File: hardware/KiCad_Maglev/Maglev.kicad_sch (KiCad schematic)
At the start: 32 parts, among them J1 USB_C_Receptacle, J2 691103110002, J3 61300621121, J4 61300821121, U1 WE-TVS-82400102, U2 ESP32-C3

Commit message: Update Rooting ESP32
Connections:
- net +USB_D: no longer U1.3, U2.25 (GPIO18/USB_D-)
- net -USB_D: no longer U1.4, U2.26 (GPIO19/USB_D+)
- new net USB_D+: U1.3, U2.25 (GPIO18/USB_D-)
- new net USB_D-: U1.4, U2.26 (GPIO19/USB_D+)
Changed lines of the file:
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@@
 	)
 	(label "I2C_INT"
-		(at 152.4 114.3 180)
+		(at 156.21 120.65 180)
 		(effects
 			(font
@@
 		)
 	)
-	(label "-USB_D"
+	(label "USB_D-"
 		(at 80.01 161.29 0)
 		(effects
@@
 	)
 	(label "EM_B_P"
-		(at 152.4 86.36 180)
+		(at 156.21 92.71 180)
 		(effects
 			(font
@@
 	)
 	(label "EM_A_N"
-		(at 152.4 81.28 180)
+		(at 156.21 87.63 180)
 		(effects
 			(font
@@
 	)
 	(label "EM_B_N"
-		(at 152.4 88.9 180)
+		(at 156.21 95.25 180)
 		(effects
 			(font
@@
 	)
 	(label "I2C_SDA"
-		(at 152.4 119.38 180)
+		(at 156.21 125.73 180)
 		(effects
 			(font
@@
 	)
 	(label "EM_C_N"
-		(at 152.4 96.52 180)
+		(at 156.21 102.87 180)
 		(effects
 			(font
@@
 		)
 	)
-	(label "+USB_D"
+	(label "USB_D+"
 		(at 81.28 179.07 0)
 		(effects
@@
 	)
 	(label "I2C_SCL"
-		(at 152.4 116.84 180)
+		(at 156.21 123.19 180)
 		(effects
 			(font
@@
 		)
 	)
-	(label "+USB_D"
+	(label "USB_D+"
 		(at 120.65 34.29 0)
 		(effects
@@
 	)
 	(label "EM_D_P"
-		(at 152.4 101.6 180)
+		(at 156.21 107.95 180)
 		(effects
 			(font
@@
 		)
 	)
-	(label "-USB_D"
+	(label "USB_D-"
 		(at 120.65 31.75 0)
 		(effects
@@
 	)
 	(label "EM_A_P"
-		(at 152.4 78.74 180)
+		(at 156.21 85.09 180)
 		(effects
 			(font
@@
 	)
 	(label "EM_C_P"
-		(at 152.4 93.98 180)
+		(at 156.21 100.33 180)
 		(effects
 			(font
@@
 	)
 	(label "EM_D_N"
-		(at 152.4 104.14 180)
+		(at 156.21 110.49 180)
 		(effects
 			(font
@@
 	(symbol
 		(lib_id "power:+3.3V")
-		(at 152.4 109.22 90)
+		(at 156.21 115.57 90)
 		(unit 1)
 		(body_style 1)
@@
 		(fields_autoplaced yes)
 		(property "Reference" "#PWR058"
-			(at 156.21 109.22 0)
+			(at 160.02 115.57 0)
 			(hide yes)
 			(show_name no)
@@
 		)
 		(property "Value" "+3.3V"
-			(at 148.59 109.22 90)
+			(at 152.4 115.57 90)
 			(show_name no)
 			(do_not_autoplace no)
@@
 		)
 		(property "Footprint" ""
-			(at 152.4 109.22 0)
+			(at 156.21 115.57 0)
 			(hide yes)
 			(show_name no)
@@
 		)
 		(property "Datasheet" ""
-			(at 152.4 109.22 0)
+			(at 156.21 115.57 0)
 			(hide yes)
 			(show_name no)
@@
 		)
 		(property "Description" "Power symbol creates a global label with name \"+3.3V\""
-			(at 152.4 109.22 0)
+			(at 156.21 115.57 0)
 			(hide yes)
 			(show_name no)
@@
 	)
 	(sheet
-		(at 152.4 74.93)
+		(at 156.21 81.28)
 		(size 40.64 50.8)
 		(exclude_from_sim no)
@@
 		)
 		(property "Sheetname" "Board to Board Connection"
-			(at 152.4 74.2184 0)
+			(at 156.21 80.5684 0)
 			(show_name no)
 			(do_not_autoplace no)
@@
 		)
 		(property "Sheetfile" "Board_to_Board_Connection.kicad_sch"
-			(at 152.4 126.3146 0)
+			(at 156.21 132.6646 0)
 			(show_name no)
 			(do_not_autoplace no)
@@
 		)
 		(pin "EM_A_N" input
-			(at 152.4 78.74 180)
+			(at 156.21 85.09 180)
 			(effects
 				(font
@@
 		)
 		(pin "EM_A_P" input
-			(at 152.4 81.28 180)
+			(at 156.21 87.63 180)
 			(effects
 				(font
@@
 		)
 		(pin "EM_B_N" input
-			(at 152.4 86.36 180)
+			(at 156.21 92.71 180)
 			(effects
 				(font
@@
 		)
 		(pin "EM_B_P" input
-			(at 152.4 88.9 180)
+			(at 156.21 95.25 180)
 			(effects
 				(font
@@
 		)
 		(pin "EM_C_N" input
-			(at 152.4 93.98 180)
+			(at 156.21 100.33 180)
 			(effects
 				(font
@@
 		)
 		(pin "EM_C_P" input
-			(at 152.4 96.52 180)
+			(at 156.21 102.87 180)
 			(effects
 				(font
@@
 		)
 		(pin "EM_D_N" input
-			(at 152.4 101.6 180)
+			(at 156.21 107.95 180)
 			(effects
 				(font
@@
 		)
 		(pin "EM_D_P" input
-			(at 152.4 104.14 180)
+			(at 156.21 110.49 180)
 			(effects
 				(font
@@
 		)
 		(pin "+3.3V" input
-			(at 152.4 109.22 180)
+			(at 156.21 115.57 180)
 			(effects
 				(font
@@
 		)
 		(pin "I2C_INT" input
-			(at 152.4 114.3 180)
+			(at 156.21 120.65 180)
 			(effects
 				(font
@@
 		)
 		(pin "I2C_SCL" input
-			(at 152.4 116.84 180)
+			(at 156.21 123.19 180)
 			(effects
 				(font
@@
 		)
 		(pin "I2C_SDA" input
-			(at 152.4 119.38 180)
+			(at 156.21 125.73 180)
 			(effects
 				(font

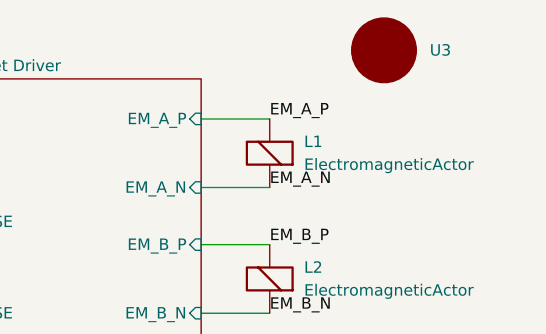
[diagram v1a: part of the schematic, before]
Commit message: Mistake in H-Bridge schematic - required rerouting
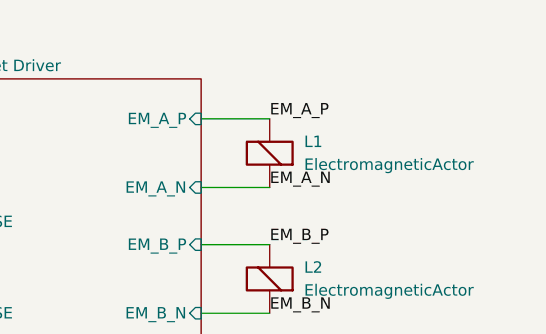
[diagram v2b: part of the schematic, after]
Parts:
- removed U3: (no value), CUSTOM:MagnetRing, symbol CUSTOM:MagnetRing
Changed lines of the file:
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@@
-	)
-	(symbol
-		(lib_id "CUSTOM:MagnetRing")
-		(at 273.05 16.51 0)
-		(unit 1)
-		(body_style 1)
-		(exclude_from_sim no)
-		(in_bom yes)
-		(on_board yes)
-		(in_pos_files yes)
-		(dnp no)
-		(fields_autoplaced yes)
-		(property "Reference" "U3"
-			(at 278.13 16.5099 0)
-			(show_name no)
-			(do_not_autoplace no)
-			(effects
-				(font
-					(size 1.27 1.27)
-				)
-				(justify left)
-			)
-		)
-		(property "Value" ""
-			(at 273.05 16.51 0)
-			(show_name no)
-			(do_not_autoplace no)
-			(effects
-				(font
-					(size 1.27 1.27)
-				)
-			)
-		)
-		(property "Footprint" "CUSTOM:MagnetRing"
-			(at 273.05 16.51 0)
-			(hide yes)
-			(show_name no)
-			(do_not_autoplace no)
-			(effects
-				(font
-					(size 1.27 1.27)
-				)
-			)
-		)
-		(property "Datasheet" ""
-			(at 273.05 16.51 0)
-			(hide yes)
-			(show_name no)
-			(do_not_autoplace no)
-			(effects
-				(font
-					(size 1.27 1.27)
-				)
-			)
-		)
-		(property "Description" ""
-			(at 273.05 16.51 0)
-			(hide yes)
-			(show_name no)
-			(do_not_autoplace no)
-			(effects
-				(font
-					(size 1.27 1.27)
-				)
-			)
-		)
-		(instances
-			(project "Maglev"
-				(path "/cf460145-35f8-4019-907e-b966a2c32625"
-					(reference "U3")
-					(unit 1)
-				)
-			)
-		)
 	)
 	(symbol

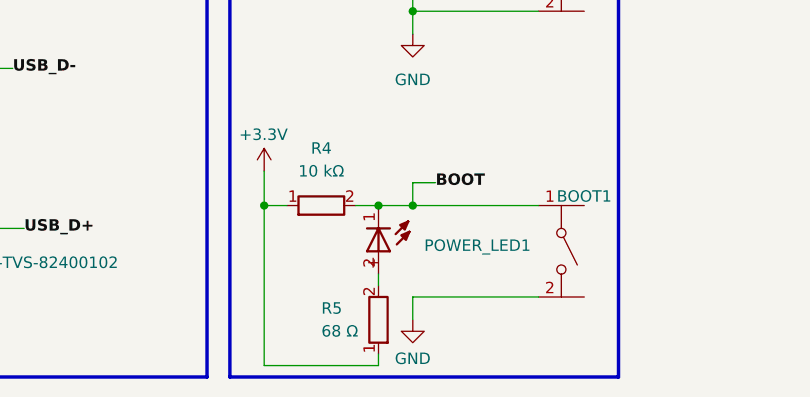
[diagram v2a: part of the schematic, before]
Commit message: Improved Silkscreen and part positioning, includes basic gerber files
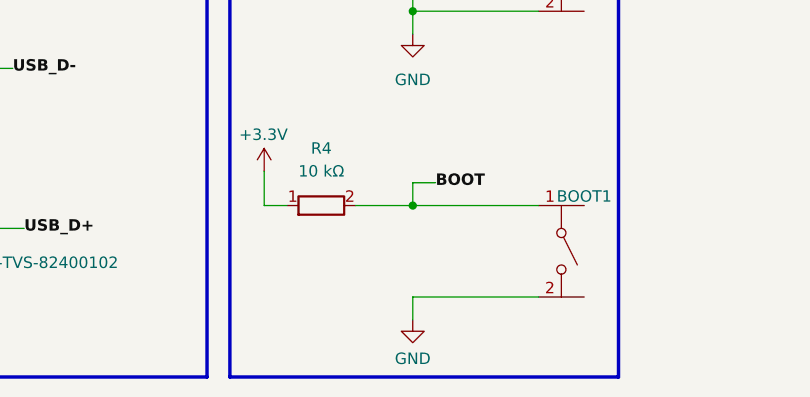
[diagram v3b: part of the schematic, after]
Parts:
- removed POWER_LED1: 0603dome_150060VS86000, LED_SMD_Wurth:D_Wurth_WL-SMCW-0603dome, symbol LED_Wurth_WL-SMCW:0603dome_150060VS86000
- removed R5: 1206_R_560112132050, Resistor_SMD_Wurth:R_Wurth_WRIS-RSKS-1206_R, symbol Resistor_Wurth_WRIS-RSKS:1206_R_560112132050

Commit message: changed usb-c connector because pcbway cant handle the old one, cleared all design rule errors
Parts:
- J1: footprint WURTH_USB:632723300011 -> WURTH_USB:629722000214
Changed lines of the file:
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@@
 			)
 		)
-		(property "Footprint" "WURTH_USB:632723300011"
+		(property "Footprint" "WURTH_USB:629722000214"
 			(at 34.29 158.75 0)
 			(hide yes)

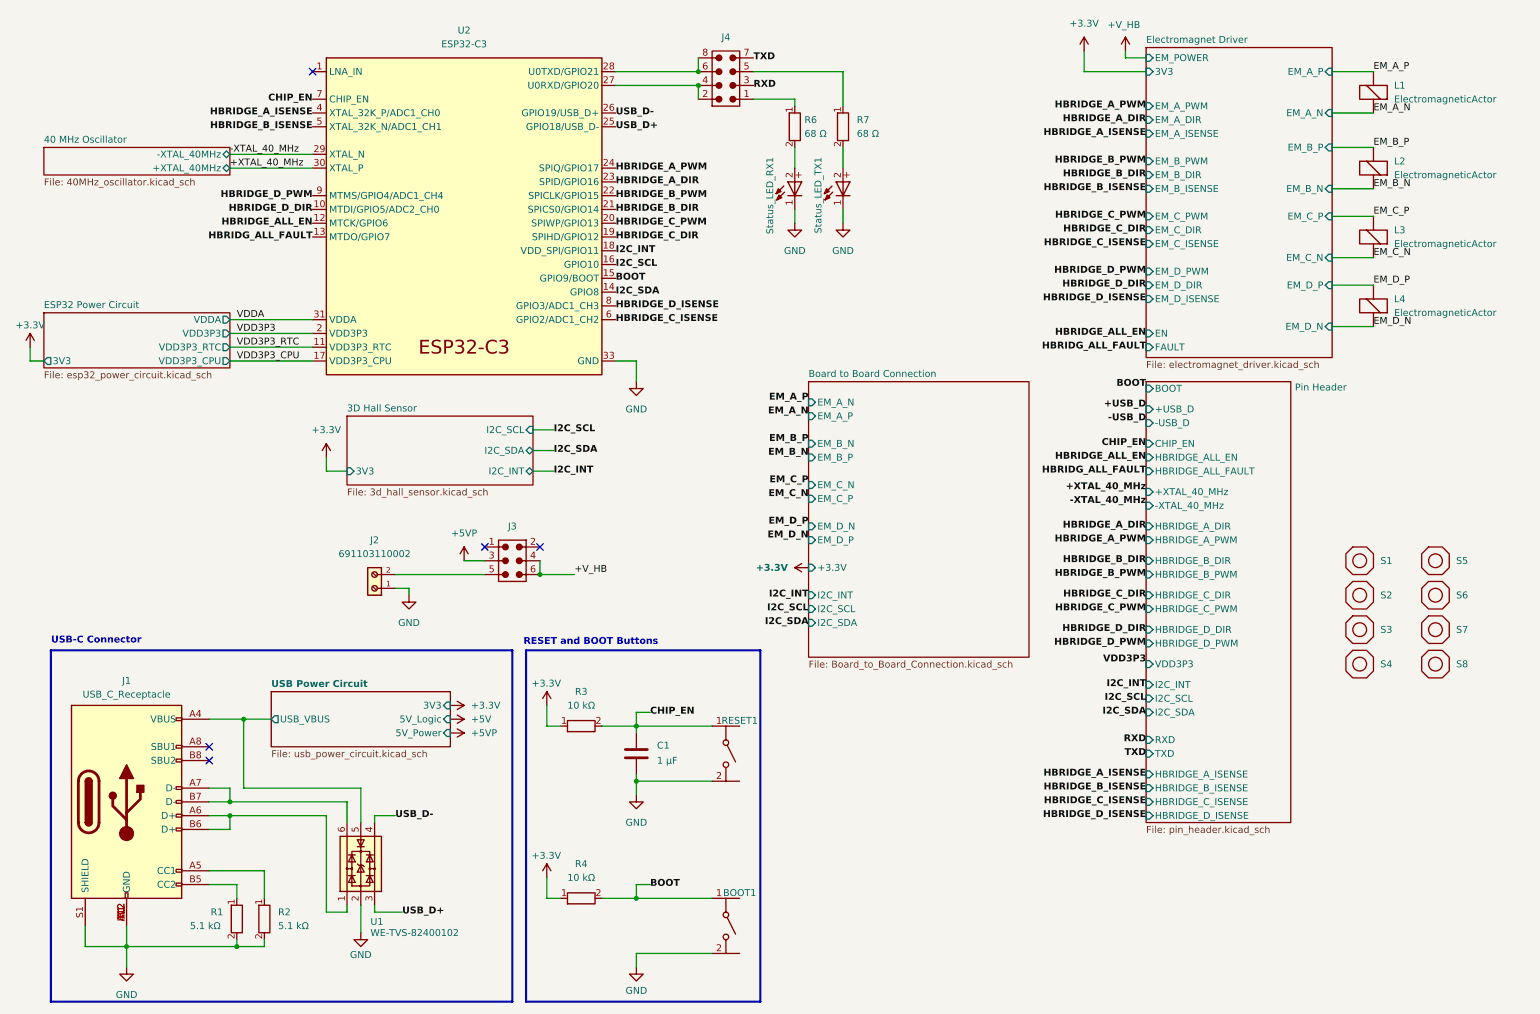
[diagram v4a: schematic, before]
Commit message: added test points in schematic
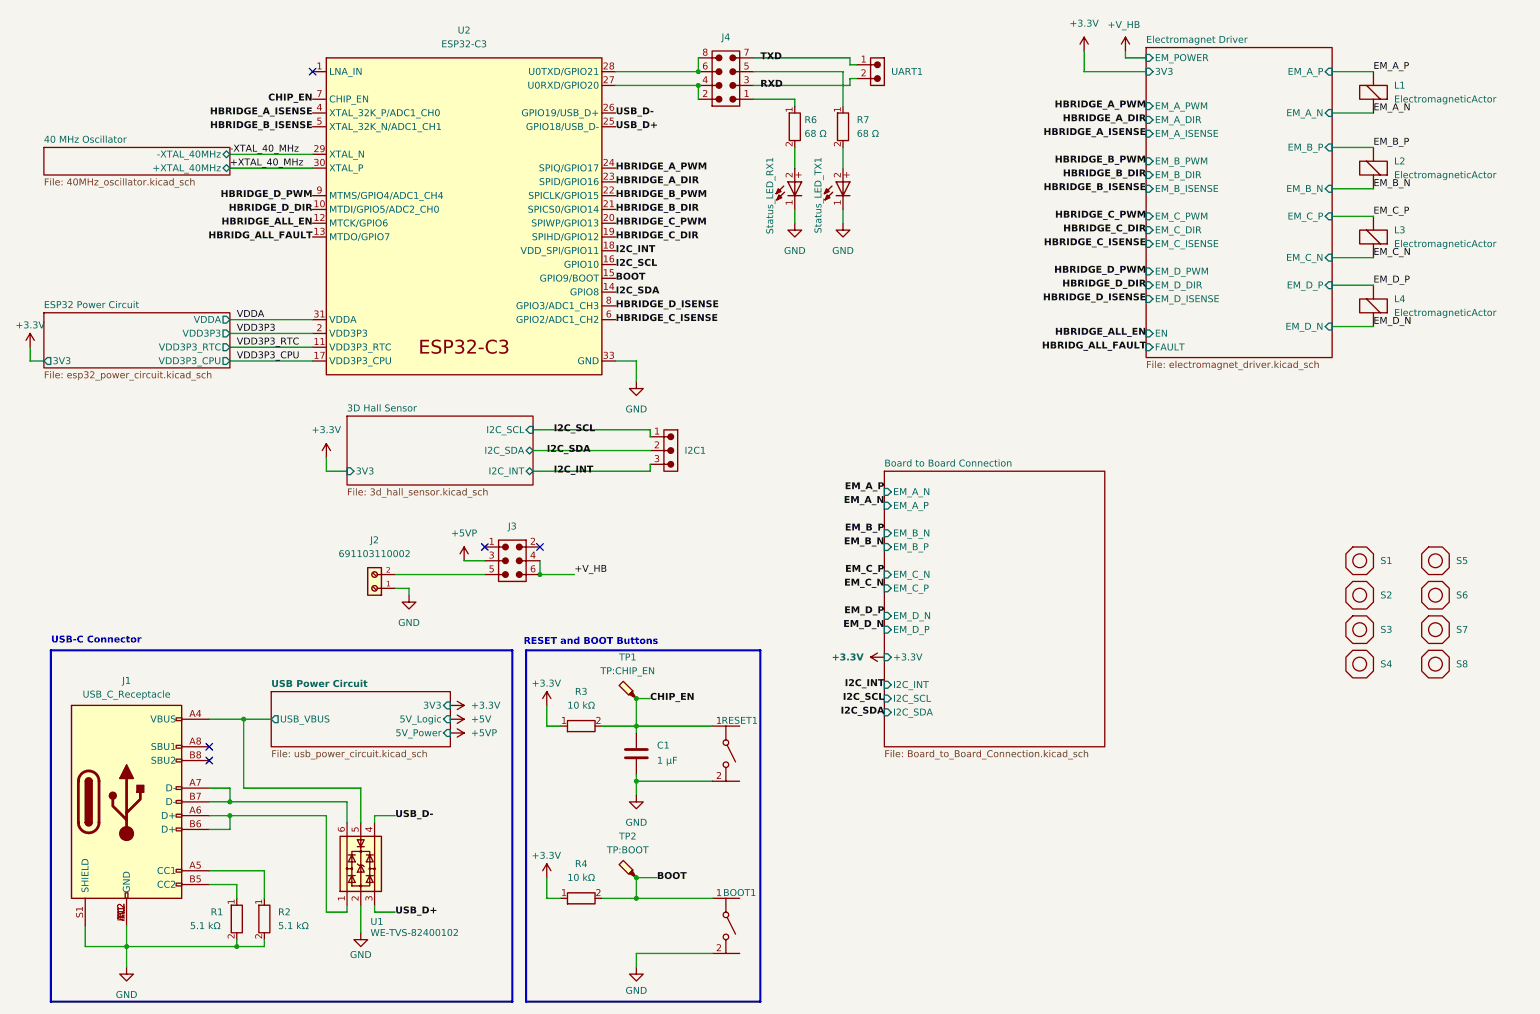
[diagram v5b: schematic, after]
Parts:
- added I2C1: 61300311121, Connector_THT_Wurth:J_Wurth_WR-PHD_61300311121, symbol Connector_Wurth_WR-PHD:61300311121
- added TP1: TP:CHIP_EN, TestPoint:TestPoint_Pad_D2.0mm, symbol Connector:TestPoint_Probe
- added TP2: TP:BOOT, TestPoint:TestPoint_Pad_D2.0mm, symbol Connector:TestPoint_Probe
- added UART1: 61300211121, Connector_THT_Wurth:J_Wurth_WR-PHD_61300211121, symbol Connector_Wurth_WR-PHD:61300211121
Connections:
- net BOOT: now also TP2.1
- net CHIP_EN: now also TP1.1
- net I2C_INT: now also I2C1.3
- net I2C_SCL: now also I2C1.1
- net I2C_SDA: now also I2C1.2
- net RXD: now also UART1.2
- net TXD: now also UART1.1
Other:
- removed sheet Pin Header
